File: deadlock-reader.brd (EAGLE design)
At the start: 49.2 x 49.5 mm, 49 parts, among them IC1 LM386M-1, IC2 STM32F072XX, IC3 MCP16301/H, IC4 MAX3232CSE, J1 RJ12 6p6c, X1 MINI-USB-SCHIELD-32005-301

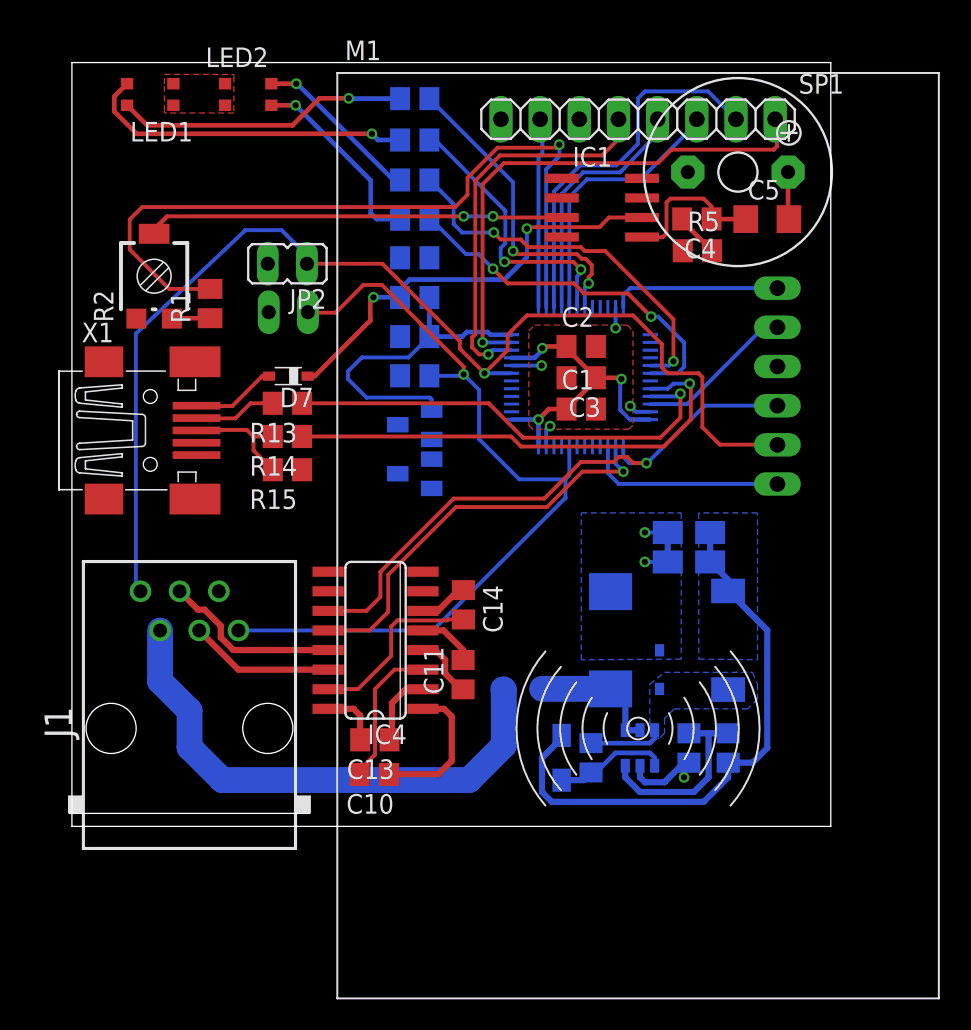
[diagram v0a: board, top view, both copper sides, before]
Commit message: [WIP] Route power distribution network
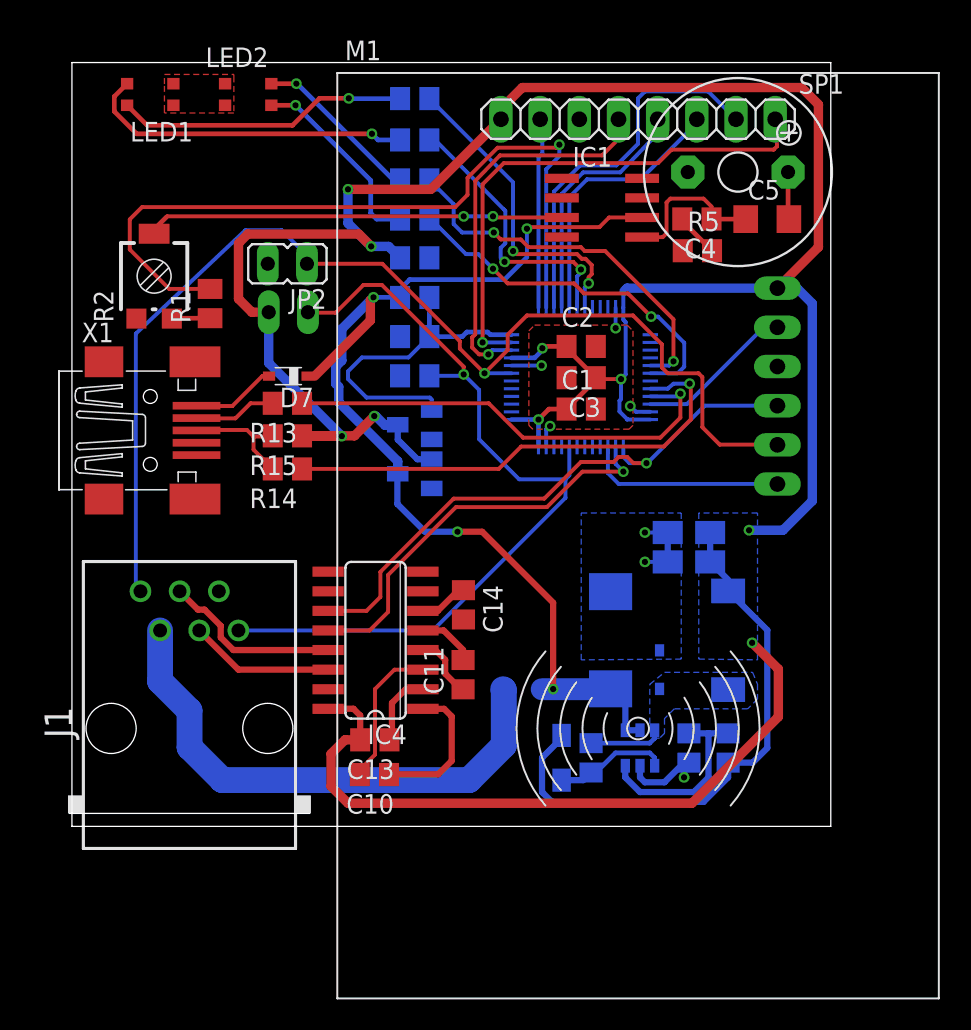
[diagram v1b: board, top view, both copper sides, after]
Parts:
- moved R15 2.20 mm to (14.0, 25.3)
- moved R14 2.10 mm to (14.0, 23.2)
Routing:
- net +3V3: track 72.6 -> 231.6 mm, vias 3 -> 9
- net V+: track 36.6 -> 71.8 mm, vias 2 -> 4
- net GND: track 28.6 -> 16.9 mm

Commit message: Create ground planes, board routing finished
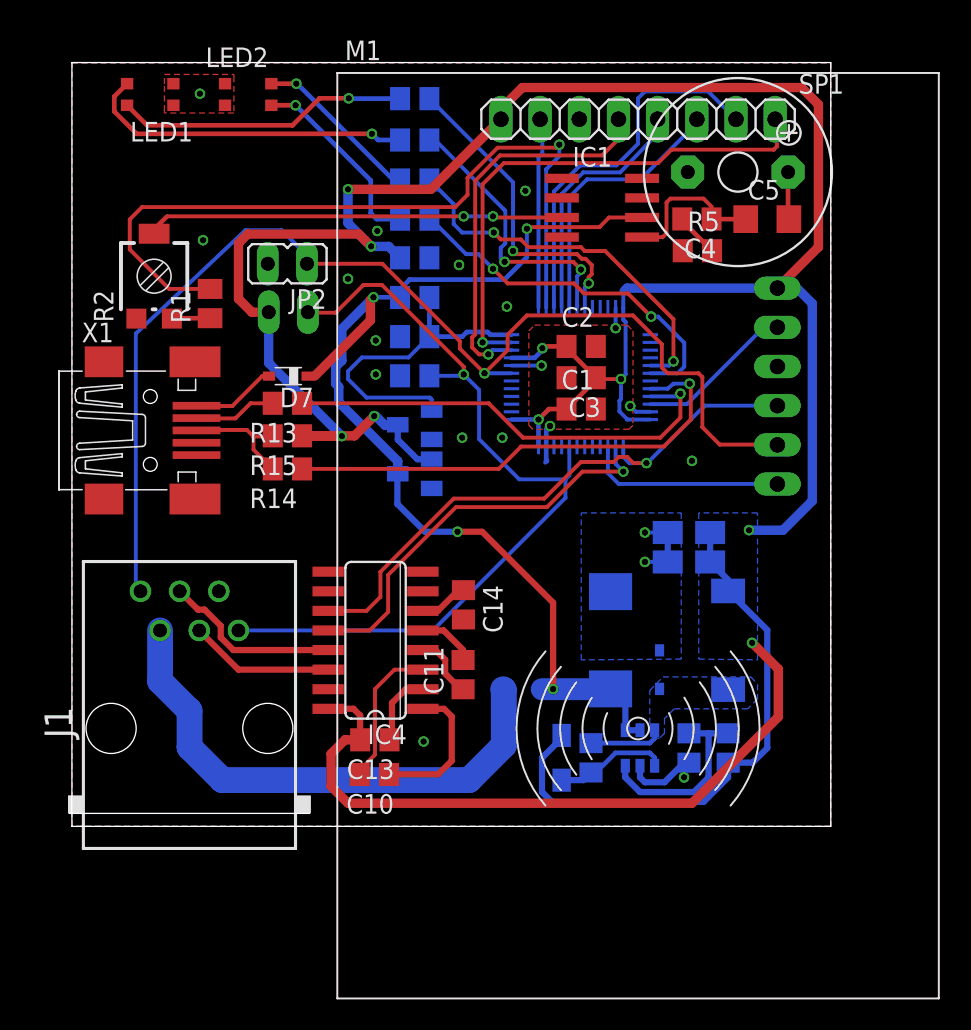
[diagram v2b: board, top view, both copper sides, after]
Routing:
- net GND: track 16.9 -> 19.1 mm, vias 7 -> 20
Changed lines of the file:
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@@
 <wire x1="37.1475" y1="19.05" x2="38.63" y2="19.05" width="0.254" layer="16"/>
 <wire x1="37.1475" y1="17.145" x2="38.63" y2="17.145" width="0.254" layer="16"/>
-<polygon width="0.4064" layer="16" spacing="0.4064" isolate="0.4064">
+<polygon width="0.4064" layer="16" spacing="0.4064" isolate="0.4064" rank="6">
 <vertex x="39.505" y="20.32"/>
 <vertex x="39.505" y="10.845"/>
@@
 <vertex x="6" y="46.375"/>
 </polygon>
-<wire x1="39.6" y1="37.32" x2="39.9288" y2="42.42" width="0" layer="19" extent="1-1"/>
-<wire x1="35.25" y1="33.625" x2="39.6" y2="37.32" width="0" layer="19" extent="1-16"/>
-<wire x1="31.765" y1="38.205" x2="35.25" y2="33.625" width="0" layer="19" extent="1-16"/>
-<wire x1="31.765" y1="40.745" x2="31.765" y2="38.205" width="0" layer="19" extent="1-1"/>
-<wire x1="32.895" y1="45.845" x2="31.765" y2="40.745" width="0" layer="19" extent="1-1"/>
-<wire x1="21.275" y1="29.21" x2="28.5" y2="29.875" width="0" layer="19" extent="16-16"/>
-<wire x1="21.275" y1="31.75" x2="21.275" y2="29.21" width="0" layer="19" extent="16-16"/>
-<wire x1="23.175" y1="36.86" x2="21.275" y2="31.75" width="0" layer="19" extent="16-16"/>
-<wire x1="37.1475" y1="19.05" x2="37.5" y2="26.875" width="0" layer="19" extent="16-16"/>
-<wire x1="39.69" y1="4.13" x2="38.1" y2="11.41" width="0" layer="19" extent="16-16"/>
-<wire x1="45.74" y1="29.815" x2="37.5" y2="26.875" width="0" layer="19" extent="16-16"/>
-<wire x1="25.385" y1="13.415" x2="34.925" y2="15.215" width="0" layer="19" extent="1-16"/>
-<wire x1="12.7" y1="36.475" x2="21.275" y2="31.75" width="0" layer="19" extent="16-16"/>
-<wire x1="7.98" y1="30.12" x2="12.7" y2="36.475" width="0" layer="19" extent="1-1"/>
-<wire x1="4.18" y1="32.92" x2="7.98" y2="30.12" width="0" layer="19" extent="1-1"/>
-<wire x1="2.08" y1="30.12" x2="4.18" y2="32.92" width="0" layer="19" extent="1-1"/>
-<wire x1="8.08" y1="24.87" x2="7.98" y2="30.12" width="0" layer="19" extent="1-1"/>
-<wire x1="8.08" y1="24.07" x2="8.08" y2="24.87" width="0" layer="19" extent="1-1"/>
-<wire x1="7.98" y1="21.22" x2="8.08" y2="24.07" width="0" layer="19" extent="1-1"/>
-<wire x1="2.08" y1="21.22" x2="7.98" y2="21.22" width="0" layer="19" extent="1-1"/>
-<wire x1="9.525" y1="15.24" x2="7.98" y2="21.22" width="0" layer="19" extent="1-1"/>
-<wire x1="16.6116" y1="8.89" x2="9.525" y2="15.24" width="0" layer="19" extent="1-1"/>
-<wire x1="9.93" y1="46.75" x2="12.7" y2="36.475" width="0" layer="19" extent="1-1"/>
+<polygon width="0.6096" layer="1" isolate="0.3048" orphans="yes">
+<vertex x="0" y="49.5"/>
+<vertex x="49.2" y="49.5"/>
+<vertex x="49.2" y="0"/>
+<vertex x="0" y="0"/>
+</polygon>
+<via x="25.1" y="36.4" extent="1-16" drill="0.4"/>
+<via x="28.2" y="33.7" extent="1-16" drill="0.4"/>
+<via x="17.9" y="35.5" extent="1-16" drill="0.4"/>
+<via x="22.8" y="5.5" extent="1-16" drill="0.4"/>
+<via x="25.3" y="25.2" extent="1-16" drill="0.4"/>
+<via x="27.9" y="25.2" extent="1-16" drill="0.4"/>
+<via x="8.5" y="38" extent="1-16" drill="0.4"/>
+<via x="8.3" y="47.5" extent="1-16" drill="0.4"/>
+<via x="19.8" y="38.6" extent="1-16" drill="0.4"/>
+<via x="19.7" y="31.5" extent="1-16" drill="0.4"/>
+<via x="19.7" y="29.3" extent="1-16" drill="0.4"/>
+<via x="40.2" y="23.7" extent="1-16" drill="0.4"/>
+<polygon width="0.3048" layer="16" isolate="0.3048" orphans="yes" rank="6">
+<vertex x="0" y="49.5"/>
+<vertex x="49.2" y="49.5"/>
+<vertex x="49.2" y="0"/>
+<vertex x="0" y="0"/>
+</polygon>
+<wire x1="30.75" y1="25.75" x2="30.75" y2="23.75" width="0.3048" layer="16"/>
+<wire x1="30.75" y1="23.75" x2="30.8" y2="23.7" width="0.3048" layer="16"/>
+<wire x1="30.8" y1="23.7" x2="30.7" y2="23.6" width="0.3048" layer="16"/>
+<via x="29.4" y="41.2" extent="1-16" drill="0.4"/>
 </signal>
 <signal name="N$1">
@@
 <wire x1="40.9575" y1="1.5875" x2="42.545" y2="3.175" width="0.4064" layer="16"/>
 <wire x1="42.545" y1="3.175" x2="42.545" y2="4.13" width="0.4064" layer="16"/>
-<polygon width="0.4064" layer="16" spacing="0.254" isolate="0.254">
+<polygon width="0.4064" layer="16" spacing="0.254" isolate="0.4064">
 <vertex x="40.64" y="20.32"/>
 <vertex x="40.64" y="10.845"/>
@@
 <wire x1="37.7825" y1="5.715" x2="37.7825" y2="6.2275" width="0.3048" layer="16"/>
 <wire x1="37.7825" y1="6.2275" x2="37.78" y2="6.23" width="0.3048" layer="16"/>
-<polygon width="0.4064" layer="16" spacing="0.254" isolate="0.254" thermals="no">
+<polygon width="0.4064" layer="16" spacing="0.254" isolate="0.6096" thermals="no">
 <vertex x="37.465" y="6.0325"/>
-<vertex x="37.465" y="9.2075"/>
-<vertex x="38.4175" y="9.985"/>
-<vertex x="44.1325" y="9.985"/>
+<vertex x="37.465" y="8.8075"/>
+<vertex x="38.3175" y="9.685"/>
+<vertex x="44.0325" y="9.685"/>
 <vertex x="44.45" y="9.2075"/>
 <vertex x="44.45" y="8.255"/>

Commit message: Incorporate revA board review fixes
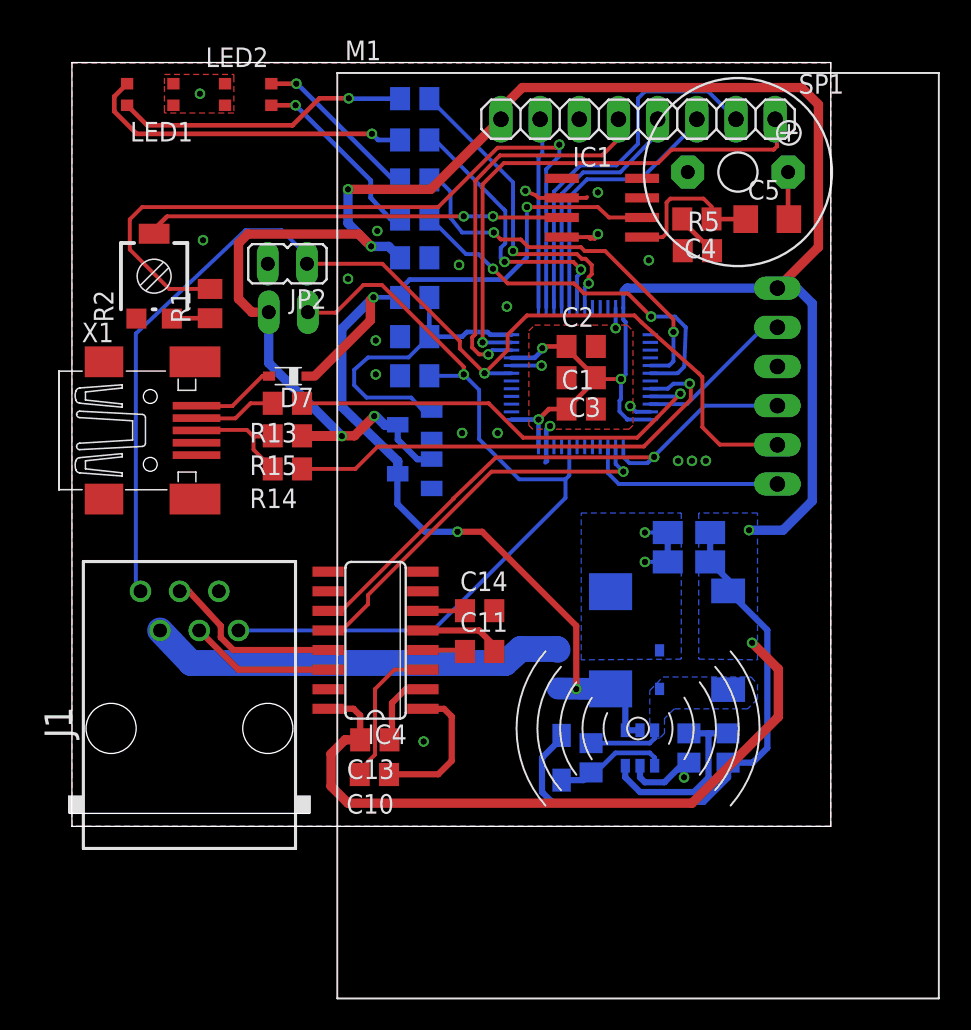
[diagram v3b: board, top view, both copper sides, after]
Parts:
- moved D5 2.62 mm to (31.5, 10.2), turned to 90 degrees
- moved C11 1.85 mm to (26.4, 11.3), turned to 0 degrees
- moved C14 1.12 mm to (26.4, 14.0), turned to 0 degrees
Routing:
- net N$9: track 34.2 -> 27.1 mm
- net GND: track 19.1 -> 25.9 mm, vias 20 -> 25
- net N$6: track 3.78 -> 5.72 mm
- net V+: track 71.8 -> 73.5 mm
- net N$5: track 4.18 -> 2.76 mm
- net RDR_RXD: track 26.6 -> 25.6 mm
- net RST: track 75.7 -> 74.7 mm
- net V_SENSE: track 21.4 -> 20.5 mm
- net USB_D-: track 29.8 -> 29.0 mm
- net USB_D+: track 31.6 -> 30.8 mm
- net LED_R2: track 23.8 -> 24.5 mm
- net AUDIO_OUT: track 49.6 -> 49.0 mm
- net N$10: track 12.6 -> 12.1 mm

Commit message: Reorganize component labels on the silkscreen
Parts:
- moved D3 5.18 mm to (39.1, 5.08), turned to 270 degrees
- moved R11 1.02 mm to (43.6, 5.08)
- moved R12 0.63 mm to (40.6, 5.08)
- moved JP1 0.14 mm to (14.0, 33.5), flipped to the top, turned to 90 degrees
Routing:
- net +3V3: track 231.6 -> 235.9 mm
- net N$25: track 12.3 -> 13.4 mm
- net GND: track 25.9 -> 26.6 mm
- net RDR_TXD/SWDIO: track 38.3 -> 37.7 mm
- net V+: track 73.5 -> 73.0 mm
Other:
- board text added: "BOOT"
- board text added: "LOCK"
- board text added: "RESET"
- board text added: "STATUS"
- board text added: "VOLUME"
